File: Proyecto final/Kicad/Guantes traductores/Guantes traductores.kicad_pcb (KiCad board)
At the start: 4 copper layers, 58 parts, among them J1 USB_C_Receptacle_USB2.0_16P, J10 Contacto1, J11 Contacto2, J12 Contacto3, J13 Contacto4, J3 Flex1, J4 Flex2, J5 Flex3, J6 Flex4, J7 Flex5, SW1 SW_SPST, SW2 SW_SPST, U1 ESP32-C3-WROOM-02, U2 ADS7128IRTER, U3 USBLC6-2SC6, U4 LMV324, U5 LMV324, U6 TPS63020, U7 TP4056 Board, U8 BNO055

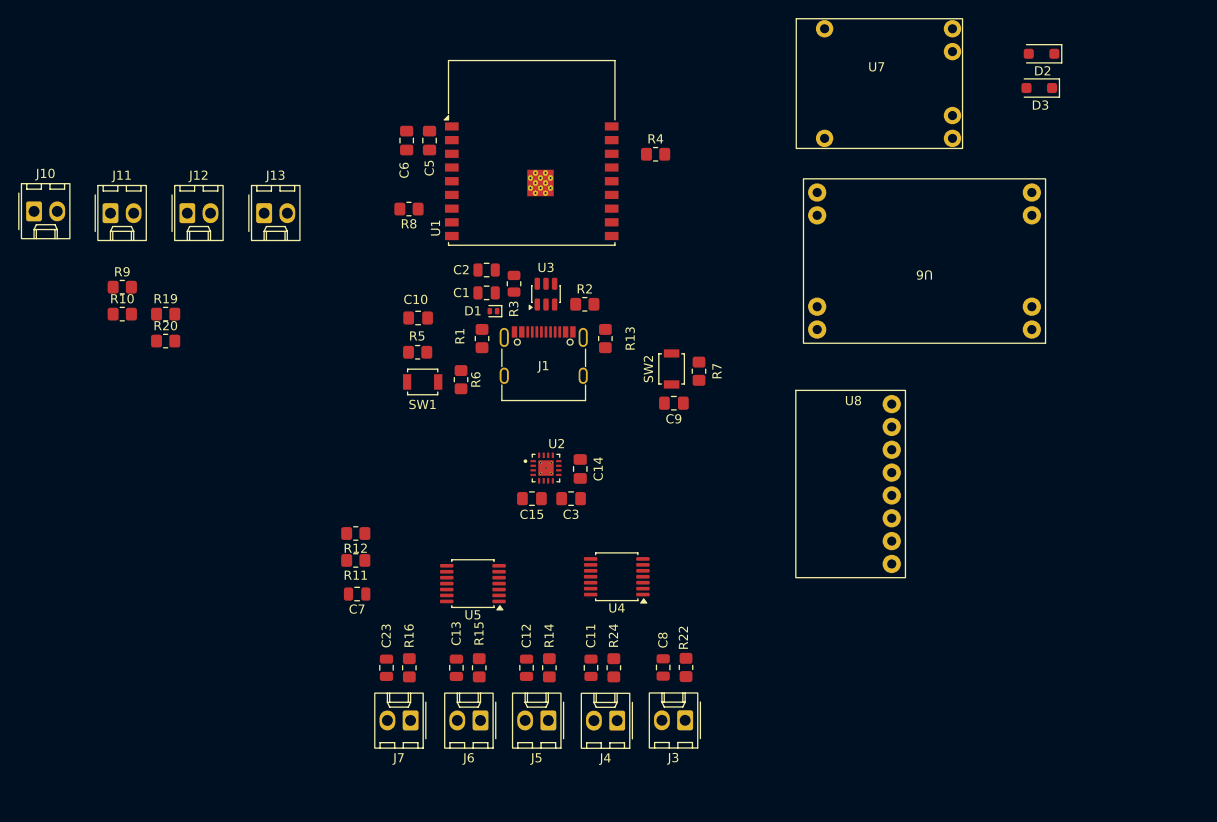
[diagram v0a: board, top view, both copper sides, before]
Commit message: Posicion de componentes
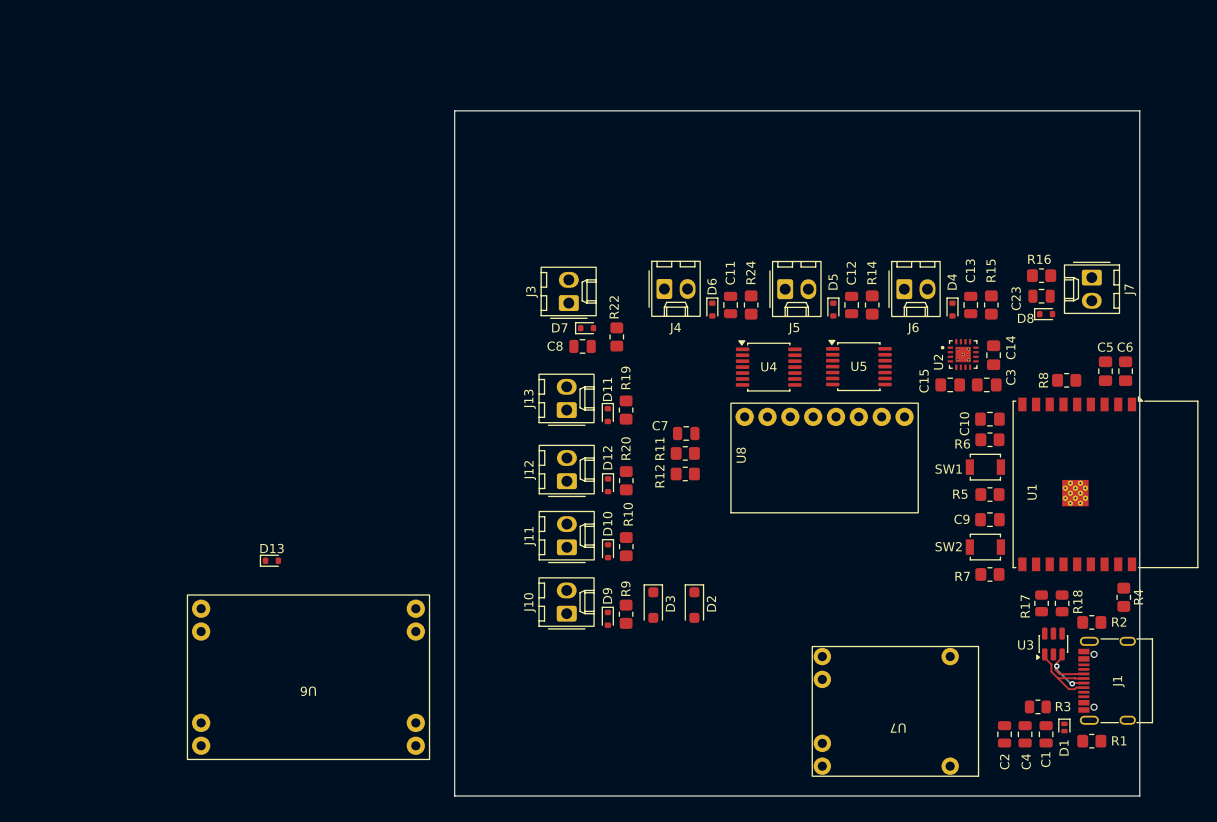
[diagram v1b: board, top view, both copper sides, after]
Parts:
- removed R13: 5.1k, Resistor_SMD:R_0805_2012Metric_Pad1.20x1.40mm_HandSolder
- added C4: 100nF, Capacitor_SMD:C_0805_2012Metric, F.Cu at (160.2, 180.5)
- added D10: ESD5B5.0ST1G, Diode_SMD:D_SOD-523, F.Cu at (114.5, 160.5)
- added D11: ESD5B5.0ST1G, Diode_SMD:D_SOD-523, F.Cu at (114.5, 145.6)
- added D12: ESD5B5.0ST1G, Diode_SMD:D_SOD-523, F.Cu at (114.5, 153.2)
- added D13: ESD5B5.0ST1G, Diode_SMD:D_SOD-523, F.Cu at (77.8, 161.5)
- added D4: ESD5B5.0ST1G, Diode_SMD:D_SOD-523, F.Cu at (152.2, 134.0)
- added D5: ESD5B5.0ST1G, Diode_SMD:D_SOD-523, F.Cu at (139.2, 134.0)
- added D6: ESD5B5.0ST1G, Diode_SMD:D_SOD-523, F.Cu at (126.0, 134.0)
- added D7: ESD5B5.0ST1G, Diode_SMD:D_SOD-523, F.Cu at (112.2, 136.0)
- added D8: ESD5B5.0ST1G, Diode_SMD:D_SOD-523, F.Cu at (162.5, 134.5)
- added D9: ESD5B5.0ST1G, Diode_SMD:D_SOD-523, F.Cu at (114.5, 167.9)
- added R17: 33, Resistor_SMD:R_0805_2012Metric, F.Cu at (162.0, 166.2)
- added R18: 33, Resistor_SMD:R_0805_2012Metric, F.Cu at (164.2, 166.2)
- moved J7 88.9 mm to (167.5, 130.5), turned to -90 degrees
- moved U7 86.2 mm to (155.0, 185.6), turned to 180 degrees
- moved C6 82.7 mm to (171.2, 140.8), turned to 90 degrees
- moved C23 82.4 mm to (162.0, 132.5), turned to 0 degrees
- moved R16 81.4 mm to (162.0, 130.3), turned to 0 degrees
- moved U6 81.4 mm to (95.0, 183.2)
- moved R1 80.0 mm to (167.5, 181.2), turned to 180 degrees
- moved C5 78.2 mm to (169.0, 140.8), turned to 90 degrees
- moved C1 78.0 mm to (162.5, 180.5), turned to -90 degrees
- moved D1 77.4 mm to (164.5, 179.8), turned to -90 degrees
- moved C2 76.1 mm to (157.9, 180.5), turned to -90 degrees
- moved R8 74.4 mm to (164.8, 141.8), turned to 0 degrees
- moved R3 73.7 mm to (161.6, 177.5), turned to 180 degrees
- moved J10 73.1 mm to (110.0, 167.3), turned to 90 degrees
- moved J1 71.7 mm to (170.4, 174.6), turned to 90 degrees
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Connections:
- net /Esp32 C3 WROOM-02/IO0 renamed IO0
- net /Esp32 C3 WROOM-02/IO1 renamed IO1
- net /Esp32 C3 WROOM-02/IO10 renamed IO10
- net /Esp32 C3 WROOM-02/IO2 renamed IO2
- net /Esp32 C3 WROOM-02/IO3 renamed IO3
- net /Esp32 C3 WROOM-02/IO4 renamed IO4
- net /Esp32 C3 WROOM-02/IO9 renamed IO9
- net /TPS4056/5VIN renamed +5V
- net 3.3V renamed +3.3V
- J1 pad S1: Net-(J1-SHIELD) -> GND
- U3 pad 4: USB_D+ -> Net-(R18-Pad1)
- U3 pad 5: unconnected-(U3-VBUS-Pad5) -> Net-(D1-K)
- U3 pad 6: USB_D- -> Net-(R17-Pad1)
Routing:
- net /USB-C/D-: track 0.00 -> 9.50 mm
- net /USB-C/D+: track 0.00 -> 9.33 mm, vias 0 -> 2
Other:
- board outline added: 75 x 75 mm

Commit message: Avance de esquematicos
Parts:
- added R13: 5.1k, Resistor_SMD:R_0805_2012Metric_Pad1.20x1.40mm_HandSolder, F.Cu at (151.4, 155.2)
- added R21: 5.1k, Resistor_SMD:R_0805_2012Metric_Pad1.20x1.40mm_HandSolder, F.Cu at (151.4, 151.5)
- moved D13 50.9 mm to (128.2, 168.9)
- moved U6 39.5 mm to (134.2, 188.0)
- moved C14 22.1 mm to (138.6, 151.6)
- moved C15 22.1 mm to (133.8, 154.8)
- moved C3 22.1 mm to (137.8, 154.8)
- moved U2 22.1 mm to (135.2, 151.5)
- moved U5 17.6 mm to (125.6, 146.8), turned to 180 degrees
- moved R5 11.5 mm to (156.4, 142.8)
- moved D3 8.54 mm to (127.7, 163.9)
- moved U8 8.21 mm to (131.3, 148.8)
- moved C7 8.17 mm to (123.5, 155.7), turned to 180 degrees
- moved D2 8.11 mm to (131.8, 164.3)
- moved U4 6.59 mm to (125.5, 140.3)
- moved R16 6.06 mm to (162.2, 136.3)
- moved SW1 5.70 mm to (155.8, 145.6)
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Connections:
- net Net-(R17-Pad1) renamed /USB-C/R-
- net Net-(R18-Pad1) renamed /USB-C/R+
- U2 pad 18: (no net) -> GND
- U2 pad 19: (no net) -> GND
- U2 pad 20: (no net) -> GND
- U2 pad 21: (no net) -> GND
- U2 pad 22: (no net) -> GND
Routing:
- net IO5: track 0.00 -> 67.3 mm, vias 0 -> 2
- net IO8: track 0.00 -> 65.8 mm, vias 0 -> 2
- net IO6: track 0.00 -> 62.7 mm, vias 0 -> 2
- net IO7: track 0.00 -> 60.4 mm, vias 0 -> 2
- net Net-(J7-Pin_2): track 0.00 -> 56.0 mm, vias 0 -> 2
- net GND: track 0.00 -> 52.2 mm, vias 0 -> 20
- net I2C_SDA: track 0.00 -> 46.6 mm, vias 0 -> 2
- net I2C_SCL: track 0.00 -> 44.7 mm, vias 0 -> 3
- net Net-(J6-Pin_2): track 0.00 -> 34.4 mm, vias 0 -> 1
- net Net-(J5-Pin_2): track 0.00 -> 23.5 mm
- net /Ads7128/AIN0: track 0.00 -> 21.3 mm, vias 0 -> 2
- net IO9: track 0.00 -> 20.4 mm
- net /Esp32 C3 WROOM-02/EN: track 0.00 -> 19.5 mm, vias 0 -> 2
- net /Ads7128/AIN3: track 0.00 -> 19.2 mm
- net /Ads7128/AIN1: track 0.00 -> 17.4 mm, vias 0 -> 2
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- added copper zone on F.Cu, net +3.3V
- added copper zone on In2.Cu, net +3.3V
- added copper zone on F.Cu, net /Ads7128/AIN0
- added copper zone on F.Cu, net /Ads7128/AIN1
- added copper zone on F.Cu, net /Ads7128/AIN2
- added copper zone on F.Cu, net /Ads7128/AIN3
- added copper zone on F.Cu, net /Ads7128/AIN4
- added copper zone on F.Cu, net /Ads7128/AIN5
- added copper zone on In1.Cu, net GND
- added copper zone on F.Cu, net Net-(D1-K)
- added copper zone on In2.Cu, net Net-(D1-K)
- added copper zone on F.Cu, net Net-(J3-Pin_2)
- added copper zone on F.Cu, net Net-(J4-Pin_2)
- added copper zone on F.Cu, net Net-(J5-Pin_2)
- added copper zone on F.Cu, net Net-(J6-Pin_2)
- added copper zone on F.Cu, net Net-(J7-Pin_2)
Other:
- board size 75 x 75 mm -> 65.3 x 54.2 mm

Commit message: Avance enrutado PF
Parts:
- moved D3 7.07 mm to (133.6, 167.8), turned to 0 degrees
- moved R7 3.80 mm to (156.3, 157.9)
- moved D2 2.07 mm to (133.6, 165.4), turned to 0 degrees
- moved SW2 2.05 mm to (155.8, 160.8)
- moved U7 1.20 mm to (154.6, 180.2)
- moved R17 0.98 mm to (161.4, 164.0)
- moved R18 0.98 mm to (161.4, 166.0)
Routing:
- net +3.3V: track 4.48 -> 36.2 mm, vias 4 -> 13
- net GND: track 52.2 -> 67.8 mm, vias 20 -> 29
- net Net-(J1-CC1): track 0.00 -> 7.55 mm
- net IO8: track 65.8 -> 68.8 mm
- net IO2: track 0.00 -> 2.41 mm
- net IO7: track 60.4 -> 62.0 mm
- net IO9: track 20.4 -> 19.4 mm
- net /USB-C/R-: track 14.4 -> 13.4 mm
- net /USB-C/R+: track 12.9 -> 11.9 mm
- net Net-(U5B-+): track 12.5 -> 13.3 mm
- added copper zone on F.Cu, net GND
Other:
- board size 65.3 x 54.2 mm -> 66.4 x 54.2 mm

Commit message: Avance enrutado pf
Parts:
- moved U7 1.18 mm to (154.6, 179.0)
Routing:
- net +3.3V: track 36.2 -> 59.4 mm, vias 13 -> 14
- net GND: track 67.8 -> 73.0 mm, vias 29 -> 32
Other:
- board size 66.4 x 54.2 mm -> 66.7 x 54.2 mm

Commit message: Enrutado TPS63020
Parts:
- removed U6: TPS63020, Custom board:TPS63020 Board
- added ?: , , F.Cu at (118.4, 173.4)
- added ?: , , F.Cu at (90.5, 159.3)
- added ?: , , F.Cu at (89.6, 159.3)
- added ?: , , F.Cu at (89.6, 160.2)
- added ?: , , F.Cu at (83.6, 159.6)
- added ?: , , F.Cu at (118.5, 175.0)
- added ?: , , F.Cu at (124.3, 175.2)
- added ?: , , F.Cu at (117.7, 175.2)
- added ?: , , F.Cu at (82.8, 160.2)
- added ?: , , F.Cu at (125.2, 175.2)
- added ?: , , F.Cu at (82.8, 159.2)
- added ?: , , F.Cu at (117.7, 173.2)
- added ?: , , F.Cu at (83.6, 160.3)
- added ?: , , F.Cu at (124.3, 173.3)
- added ?: , , F.Cu at (89.6, 161.1)
- added ?: , , F.Cu at (117.7, 174.2)
- added ?: , , F.Cu at (124.3, 174.2)
- added ?: , , F.Cu at (83.6, 161.1)
- added ?: , , F.Cu at (118.5, 174.2)
- added ?: , , F.Cu at (90.5, 161.2)
- added ?: , , F.Cu at (125.2, 173.3)
- added ?: , , F.Cu at (90.5, 160.3)
- added ?: , , F.Cu at (82.8, 161.2)
- added ?: , , F.Cu at (125.2, 174.3)
- added C1: 10uf, Capacitor_SMD:C_0805_2012Metric_Pad1.18x1.45mm_HandSolder, F.Cu at (85.4, 168.8)
- added C16: 10uf, Capacitor_SMD:C_0805_2012Metric_Pad1.18x1.45mm_HandSolder, F.Cu at (129.4, 177.8)
- added C17: 10uf, Capacitor_SMD:C_0805_2012Metric_Pad1.18x1.45mm_HandSolder, F.Cu at (127.2, 177.8)
- added C18: 100nf, Capacitor_SMD:C_0805_2012Metric_Pad1.18x1.45mm_HandSolder, F.Cu at (125.1, 177.8)
- added C19: 22uf, Capacitor_SMD:C_0805_2012Metric_Pad1.18x1.45mm_HandSolder, F.Cu at (124.8, 170.7)
- added C2: 10uf, Capacitor_SMD:C_0805_2012Metric_Pad1.18x1.45mm_HandSolder, F.Cu at (85.4, 166.2)
- added C20: 22uf, Capacitor_SMD:C_0805_2012Metric_Pad1.18x1.45mm_HandSolder, F.Cu at (124.8, 166.2)
- added C21: 22uf, Capacitor_SMD:C_0805_2012Metric_Pad1.18x1.45mm_HandSolder, F.Cu at (124.8, 168.5)
- added C3: 100nf, Capacitor_SMD:C_0805_2012Metric_Pad1.18x1.45mm_HandSolder, F.Cu at (85.6, 163.9)
- added C4: 22uf, Capacitor_SMD:C_0805_2012Metric_Pad1.18x1.45mm_HandSolder, F.Cu at (86.1, 155.7)
- added C5: 22uf, Capacitor_SMD:C_0805_2012Metric_Pad1.18x1.45mm_HandSolder, F.Cu at (86.1, 152.8)
- added C6: 22uf, Capacitor_SMD:C_0805_2012Metric_Pad1.18x1.45mm_HandSolder, F.Cu at (86.1, 150.0)
- added L1: 1.5uH, Inductor_SMD:L_APV_APH0630, F.Cu at (78.7, 160.3)
- added L1: 1.5uH, Inductor_SMD:L_APV_APH0630, F.Cu at (113.6, 174.2)
- added R1: 1M, Resistor_SMD:R_0805_2012Metric_Pad1.20x1.40mm_HandSolder, F.Cu at (89.5, 148.8)
- added R2: 180K, Resistor_SMD:R_0805_2012Metric_Pad1.20x1.40mm_HandSolder, F.Cu at (86.1, 147.4)
- added R23: 1M, Resistor_SMD:R_0805_2012Metric_Pad1.20x1.40mm_HandSolder, F.Cu at (124.7, 161.8)
- added R25: 180K, Resistor_SMD:R_0805_2012Metric_Pad1.20x1.40mm_HandSolder, F.Cu at (128.8, 161.8)
- added R26: 1M, Resistor_SMD:R_0805_2012Metric_Pad1.20x1.40mm_HandSolder, F.Cu at (124.7, 164.0)
- added R3: 1M, Resistor_SMD:R_0805_2012Metric_Pad1.20x1.40mm_HandSolder, F.Cu at (90.4, 152.7)
- added U10: TPS63020DSJR, Custom board:IC_TPS63020DSJR, F.Cu at (121.3, 174.2)
- added U9: TPS63020DSJR, tps63020:TPS63020DSJR, F.Cu at (86.6, 160.2)
- moved D13 29.1 mm to (134.1, 140.5), turned to 180 degrees
- moved D3 11.0 mm to (133.7, 178.8)
- moved D2 9.51 mm to (132.6, 174.8), turned to 90 degrees
- moved U7 1.33 mm to (154.6, 180.3)
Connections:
- U2 pad 18: GND -> (no net)
- U2 pad 19: GND -> (no net)
- U2 pad 20: GND -> (no net)
- U2 pad 21: GND -> (no net)
- U2 pad 22: GND -> (no net)
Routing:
- net VBat: track 0.00 -> 29.7 mm, vias 0 -> 1
- net +3.3V: track 59.4 -> 84.1 mm, vias 14 -> 15
- net Net-(U10-PG): track 0.00 -> 18.4 mm, vias 0 -> 2
- net Net-(U2-FB): track 0.00 -> 17.7 mm, vias 0 -> 2
- net Net-(U10-FB): track 0.00 -> 17.2 mm, vias 0 -> 2
- net VBAT: track 0.00 -> 15.8 mm, vias 0 -> 3
- net Net-(U2-PG): track 0.00 -> 13.9 mm
- net /Ads7128/AIN5: track 0.00 -> 13.7 mm, vias 0 -> 2
- net GND: track 73.0 -> 84.1 mm, vias 32 -> 61
- net /Buckboost 3.7V-5V a 3.3V/Vin: track 0.00 -> 5.62 mm, vias 0 -> 2
- net IO6: track 62.7 -> 64.2 mm
- net IO5: track 67.3 -> 68.7 mm, vias 2 -> 3
- net /Esp32 C3 WROOM-02/EN: track 19.5 -> 18.4 mm
- net +3V3: vias 0 -> 1
- added copper zone on F.Cu, net +3V3
- added copper zone on F.Cu, net +5V
- added copper zone on F.Cu, net /Buckboost 3.7V-5V a 3.3V/Vin
- added copper zone on F.Cu, net Net-(D3-A)
- added copper zone on F.Cu, net Net-(U10-L1_8)
- added copper zone on F.Cu, net Net-(U10-L2_6)
- added copper zone on F.Cu, net Net-(U2-L1_8)
- added copper zone on F.Cu, net Net-(U2-L2_6)
- added copper zone on F.Cu, net VBAT

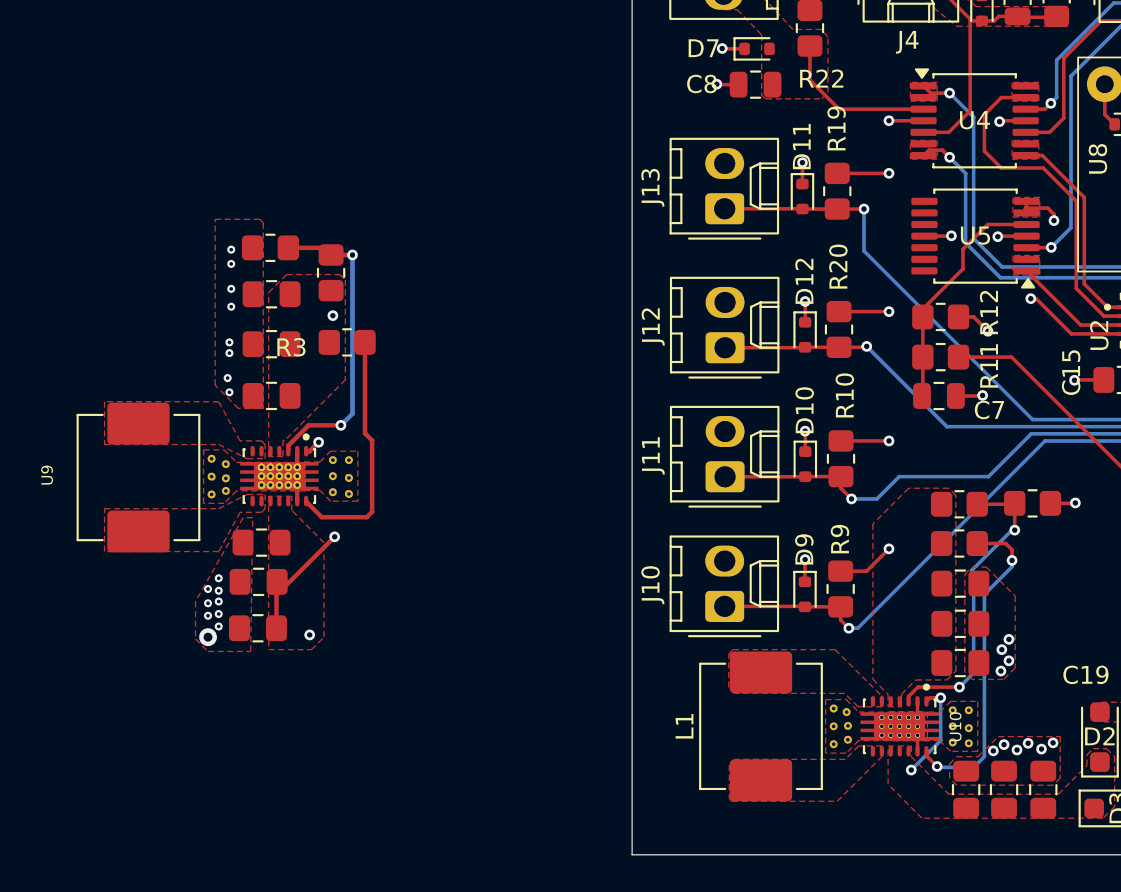
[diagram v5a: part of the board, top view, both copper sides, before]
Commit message: Enrutado TPS63020 y correccion de DRC
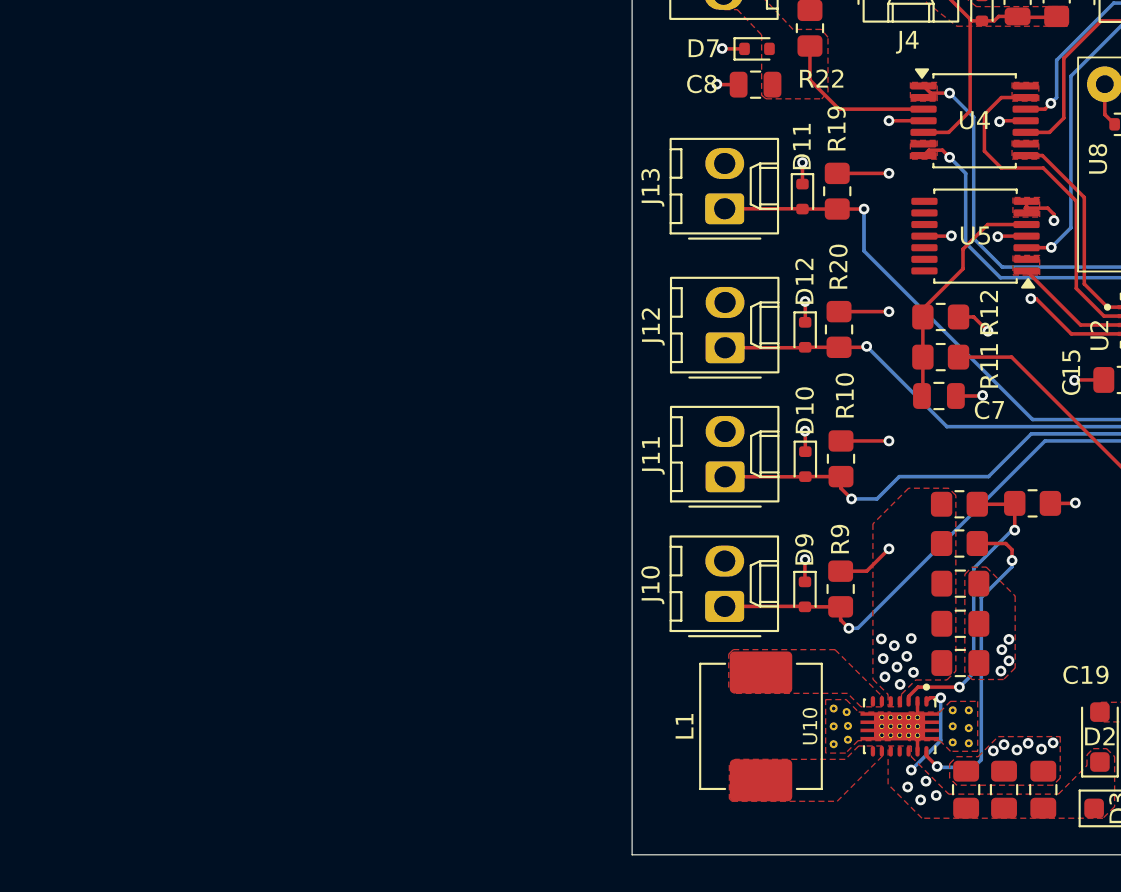
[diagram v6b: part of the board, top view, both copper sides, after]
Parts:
- removed the ? at (90.5, 159.3)
- removed the ? at (89.6, 159.3)
- removed the ? at (89.6, 160.2)
- removed the ? at (83.6, 159.6)
- removed the ? at (82.8, 160.2)
- removed the ? at (82.8, 159.2)
- removed the ? at (83.6, 160.3)
- removed the ? at (89.6, 161.1)
- removed the ? at (83.6, 161.1)
- removed the ? at (90.5, 161.2)
- removed the ? at (90.5, 160.3)
- removed the ? at (82.8, 161.2)
- removed the C1 at (85.4, 168.8)
- removed the C2 at (85.4, 166.2)
- removed the C3 at (85.6, 163.9)
- removed the C4 at (86.1, 155.7)
- removed the C5 at (86.1, 152.8)
- removed the C6 at (86.1, 150.0)
- removed the L1 at (78.7, 160.3)
- removed the R1 at (89.5, 148.8)
- removed the R2 at (86.1, 147.4)
- removed the R3 at (90.4, 152.7)
- removed U9: TPS63020DSJR, tps63020:TPS63020DSJR
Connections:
- U2 pad 18: (no net) -> GND
- U2 pad 19: (no net) -> GND
- U2 pad 20: (no net) -> GND
- U2 pad 21: (no net) -> GND
- U2 pad 22: (no net) -> GND
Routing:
- net Net-(U2-FB): track 17.7 -> 0.00 mm, vias 2 -> 0
- net VBAT: track 15.8 -> 0.00 mm, vias 3 -> 0
- net Net-(U2-PG): track 13.9 -> 0.00 mm
- net GND: track 84.1 -> 81.4 mm, vias 61 -> 45
- net IO5: vias 3 -> 2
- net /Buckboost 3.7V-5V a 3.3V/Vin: vias 2 -> 6
- net +3V3: vias 1 -> 0
- net +3.3V: vias 15 -> 24
- added copper zone on In2.Cu, net /Buckboost 3.7V-5V a 3.3V/Vin
- removed copper zone on F.Cu, net +3V3
- removed copper zone on F.Cu, net Net-(U2-L1_8)
- removed copper zone on F.Cu, net Net-(U2-L2_6)
- removed copper zone on F.Cu, net VBAT

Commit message: Added TVS diodes in i2c channels
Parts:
- added D14: ESD5B5.0ST1G, Diode_SMD:D_SOD-523, F.Cu at (137.2, 140.6)
- added D15: ESD5B5.0ST1G, Diode_SMD:D_SOD-523, F.Cu at (141.1, 140.6)
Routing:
- net GND: track 81.4 -> 85.6 mm, vias 45 -> 47
- net I2C_SCL: track 44.6 -> 46.9 mm
- added copper zone on B.Cu, net GND
